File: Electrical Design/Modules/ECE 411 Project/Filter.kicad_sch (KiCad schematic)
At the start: 2 parts

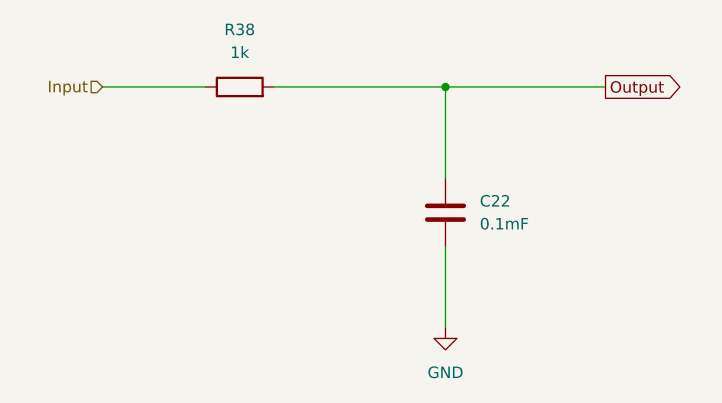
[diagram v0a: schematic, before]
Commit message: Final Touches to Preliminary Schematic
Created Symbol for Small OLED screen and finalized input/output connections for each module
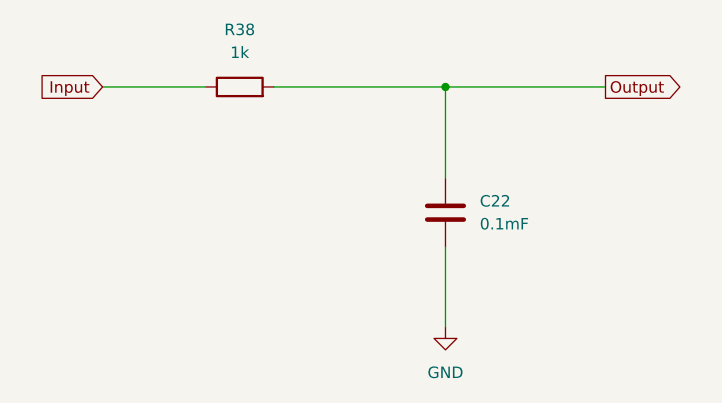
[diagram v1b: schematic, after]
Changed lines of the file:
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@@
+		)
+	)
+	(global_label "Input"
+		(shape input)
+		(at 82.55 76.2 180)
+		(fields_autoplaced yes)
+		(effects
+			(font
+				(size 1.27 1.27)
+			)
+			(justify right)
+		)
+		(property "Intersheetrefs" "${INTERSHEET_REFS}"
+			(at 74.7873 76.2 0)
+			(effects
+				(font
+					(size 1.27 1.27)
+				)
+				(justify right)
+				(hide yes)
+			)
 		)
 	)
@@
 		)
 	)
-	(hierarchical_label "Input"
-		(shape input)
-		(at 82.55 76.2 180)
-		(fields_autoplaced yes)
-		(effects
-			(font
-				(size 1.27 1.27)
-			)
-			(justify right)
-		)
-	)

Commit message: kicad business
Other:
- company: (none) -> Portland State University
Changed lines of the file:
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@@
 	(generator_version "8.0")
 	(paper "A4")
+	(title_block
+		(company "Portland State University")
+		(comment 1 "Open Source Hardware")
+		(comment 2 "Design: Eric Sanman, Sierra Buckley, Chuong Vo, Chris Crider")
+	)
 	(junction
 		(at 120.65 76.2)
